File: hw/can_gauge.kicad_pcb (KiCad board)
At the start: 2 copper layers, 28 parts, among them J1 Gauge 1, J2 Gauge 2, J3 Gauge 3, J4 Gauge 4, J5 Gauge 5, J6 Gauge 6, J7 Power & CAN, U1 PIC16F1459-IP, U2 MCP2515-xST, U3 MCP2561T-E/SN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

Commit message: hw: partial uc layout
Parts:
- removed U3: MCP2561T-E/SN, Package_SO:SOIC-8_3.9x4.9mm_P1.27mm
- added XCVR1: MCP2561-E-P, Package_DIP:DIP-8_W7.62mm, F.Cu at (122.3, 133.2)
- U2: value MCP2515-xST -> ~; footprint Package_SO:TSSOP-20_4.4x6.5mm_P0.65mm -> Package_DIP:DIP-18_W7.62mm
- moved C1 120.2 mm to (96.0, 150.7), turned to -90 degrees
- moved Vreg1 106.4 mm to (91.5, 152.5), turned to -90 degrees
- moved C3 100.6 mm to (80.4, 151.8), turned to -90 degrees
- moved C2 98.2 mm to (85.5, 151.8), turned to -90 degrees
- moved C4 75.6 mm to (92.0, 113.5)
- moved C5 65.9 mm to (117.0, 130.0), turned to 180 degrees
- moved U2 61.2 mm to (122.5, 126.0), turned to 180 degrees
- moved C6 56.2 mm to (119.5, 130.0)
- moved R1 39.1 mm to (156.0, 112.0)
- moved U1 35.3 mm to (91.9, 117.2)
- moved C7 0.50 mm to (86.5, 125.0)
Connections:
- J7 pad 1: CAN_H -> GND
- J7 pad 2: GND -> CAN_H
- J7 pad 3: CAN_L -> +12V
- J7 pad 4: +12V -> CAN_L
- U2 pad 10: GND -> unconnected-(U2-~{RX1BF}-Pad10)
- U2 pad 12: unconnected-(U2-~{RX0BF}-Pad12) -> ~{INT}
- U2 pad 13: ~{INT} -> SCK
- U2 pad 14: SCK -> SO
- U2 pad 15: unconnected-(U2-NC-Pad15) -> SI
- U2 pad 16: SO -> ~{CS}
- U2 pad 17: SI -> Net-(U2-~{RESET})
- U2 pad 18: ~{CS} -> +5V
- U2 pad 8: unconnected-(U2-OSC2-Pad8) -> CLK
- U2 pad 9: CLK -> GND
- Vreg1 pad 4: (no net) -> GND
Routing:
- net Net-(U4-QH'): track 0.00 -> 42.3 mm
- net Net-(U1-CWG1B/C1OUT/C2OUT/RC4): track 0.00 -> 37.0 mm
- net Net-(U1-PWM1/CWG1A/T0CKI/RC5): track 0.00 -> 35.2 mm
- net Net-(U1-CLKR/C1IN3-/C2IN3-/DACOUT2/AN7/RC3): track 0.00 -> 24.5 mm
- net RX: track 0.00 -> 20.4 mm
- net +5V: track 118.5 -> 137.5 mm
- net GND: track 12.1 -> 1.94 mm, vias 12 -> 23
- net TX: track 0.00 -> 8.06 mm

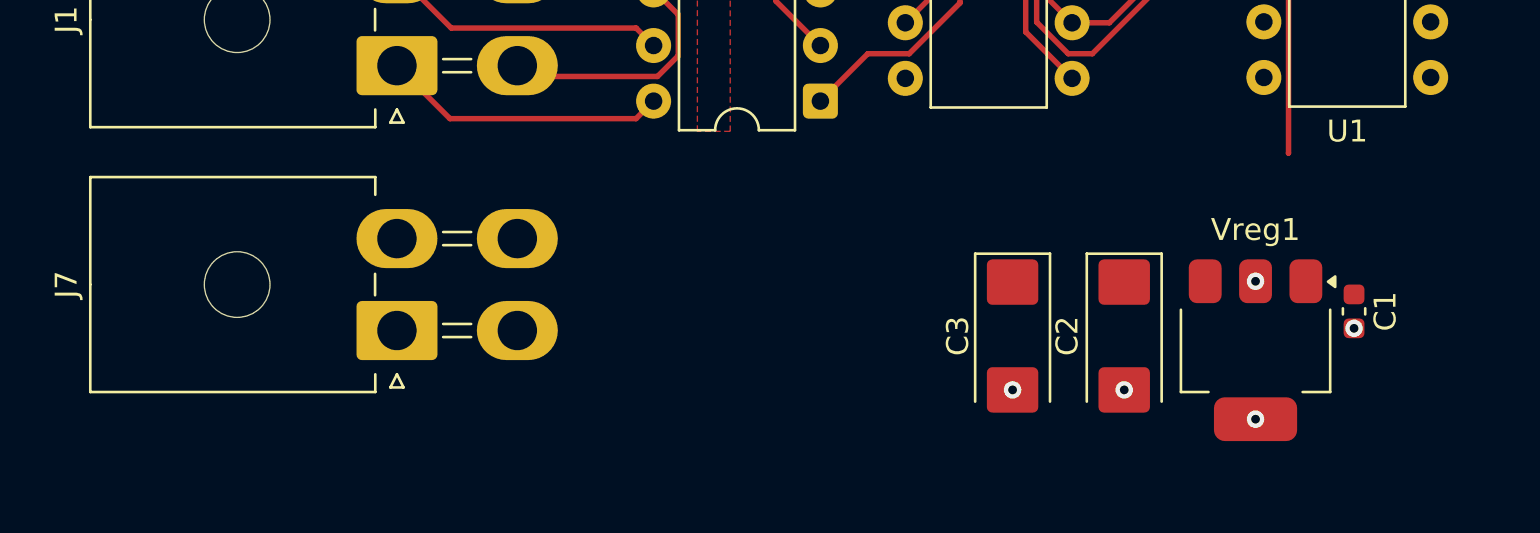
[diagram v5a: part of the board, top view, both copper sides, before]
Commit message: hw: vreg placement
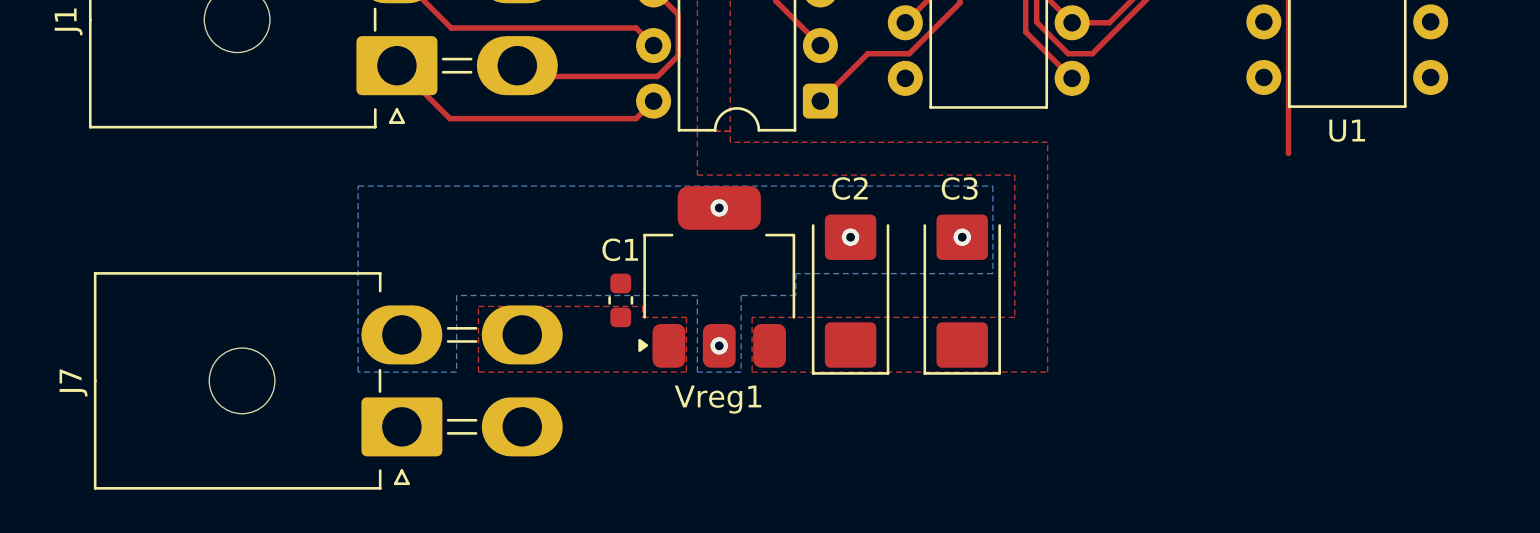
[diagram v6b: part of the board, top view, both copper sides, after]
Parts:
- moved C1 33.5 mm to (62.5, 150.2), turned to 90 degrees
- moved Vreg1 24.7 mm to (67.0, 149.2), turned to 90 degrees
- moved C2 12.7 mm to (73.0, 149.8), turned to 90 degrees
- moved J7 4.41 mm to (52.5, 156.0)
- moved C3 3.08 mm to (78.1, 149.8), turned to 90 degrees
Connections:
- J7 pad 1: GND -> CAN_H
- J7 pad 2: CAN_H -> GND
- J7 pad 3: +12V -> CAN_L
- J7 pad 4: CAN_L -> +12V
- Vreg1 pad 4: GND -> (no net)
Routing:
- added copper zone on F.Cu, net +12V
- added copper zone on B.Cu, net GND

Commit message: hw: data traces
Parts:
- moved C8 10.1 mm to (78.0, 95.5), turned to 180 degrees
- moved C3 0.60 mm to (77.5, 149.8)
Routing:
- net Net-(U5-QH'): track 0.00 -> 39.6 mm
- net Net-(U1-PWM1/CWG1A/T0CKI/RC5): track 35.2 -> 61.7 mm
- net Net-(U1-CWG1B/C1OUT/C2OUT/RC4): track 37.0 -> 62.4 mm
- net +5V: track 137.5 -> 128.3 mm

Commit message: hw: move shift register and position xcvr
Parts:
- moved C4 42.6 mm to (93.0, 71.0)
- moved U1 42.6 mm to (92.9, 74.6)
- moved XCVR1 37.2 mm to (92.5, 155.5), turned to 180 degrees
- moved C6 31.6 mm to (95.5, 150.5), turned to -90 degrees
- moved C5 10.3 mm to (123.5, 138.0)
- moved C7 9.86 mm to (78.0, 120.0), turned to 180 degrees
- moved U4 0.92 mm to (75.5, 123.2)
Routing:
- net +5V: track 128.3 -> 75.7 mm
- net Net-(U4-QH'): track 42.3 -> 0.00 mm
- net Net-(U1-CWG1B/C1OUT/C2OUT/RC4): track 62.4 -> 25.2 mm
- net Net-(U1-PWM1/CWG1A/T0CKI/RC5): track 61.7 -> 26.2 mm
- net CAN_H: track 0.00 -> 35.3 mm
- net CAN_L: track 0.00 -> 30.2 mm
- net Net-(U1-CLKR/C1IN3-/C2IN3-/DACOUT2/AN7/RC3): track 24.5 -> 0.00 mm
- net RX: track 20.4 -> 0.00 mm
- net TX: track 8.06 -> 0.27 mm
- net GND: track 1.48 -> 0.50 mm, vias 23 -> 20
